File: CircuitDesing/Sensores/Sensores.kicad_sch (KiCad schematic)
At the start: 6 parts

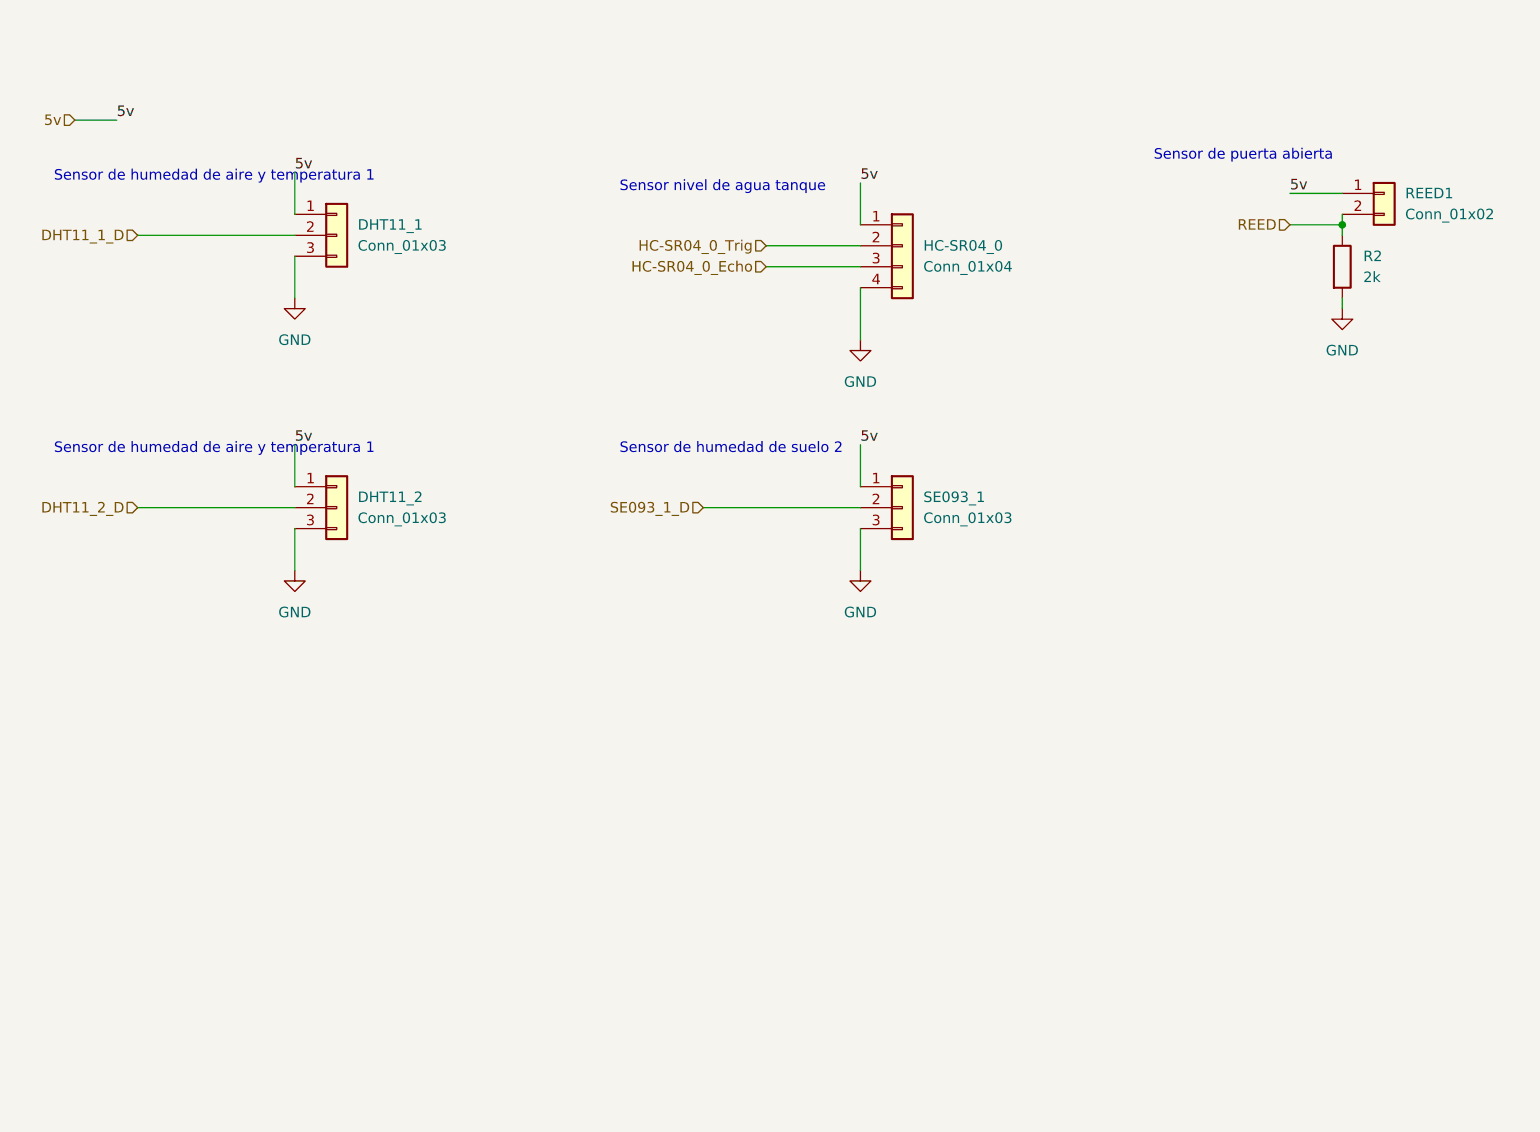
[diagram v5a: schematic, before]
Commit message: Listo para Ruteo
Cambios en programador, led usuario, pines 34 35 (solo entrada)
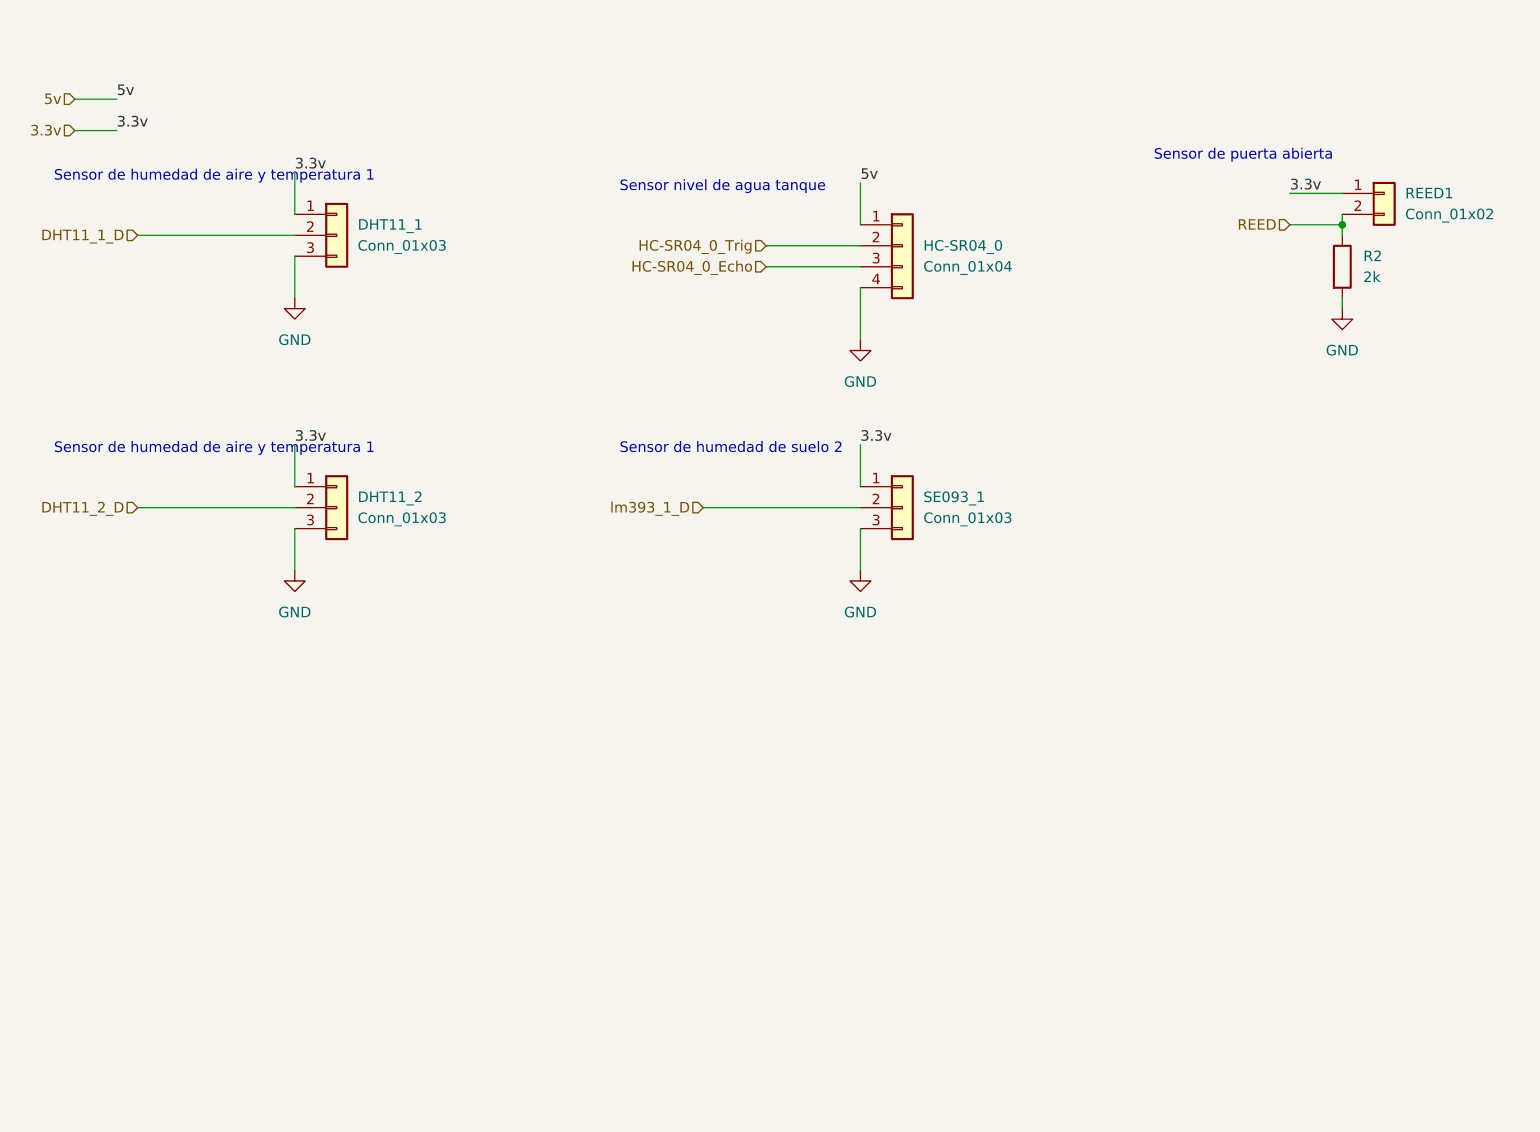
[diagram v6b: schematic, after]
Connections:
- net 5v: no longer DHT11_1.1 (Pin_1), DHT11_2.1 (Pin_1), REED1.1 (Pin_1), SE093_1.1 (Pin_1)
- net SE093_1_D renamed lm393_1_D
- new net 3.3v: DHT11_1.1 (Pin_1), DHT11_2.1 (Pin_1), REED1.1 (Pin_1), SE093_1.1 (Pin_1)
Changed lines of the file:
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@@
+    (stroke (width 0) (type default) (color 0 0 0 0))
+  )
+  (wire (pts (xy 43.18 52.07) (xy 48.26 52.07))
     (stroke (width 0) (type default) (color 0 0 0 0))
   )
@@
     (stroke (width 0) (type default) (color 0 0 0 0))
   )
-  (wire (pts (xy 43.18 50.8) (xy 48.26 50.8))
+  (wire (pts (xy 43.18 48.26) (xy 48.26 48.26))
     (stroke (width 0) (type default) (color 0 0 0 0))
   )
@@
     (effects (font (size 1.27 1.27)) (justify left bottom))
   )
-  (label "5v" (at 48.26 50.8 0)
+  (label "3.3v" (at 48.26 52.07 0)
     (effects (font (size 1.27 1.27)) (justify left bottom))
   )
-  (label "5v" (at 69.85 57.15 0)
+  (label "5v" (at 48.26 48.26 0)
     (effects (font (size 1.27 1.27)) (justify left bottom))
   )
-  (label "5v" (at 69.85 90.17 0)
+  (label "3.3v" (at 69.85 57.15 0)
     (effects (font (size 1.27 1.27)) (justify left bottom))
   )
-  (label "5v" (at 138.43 90.17 0)
+  (label "3.3v" (at 69.85 90.17 0)
     (effects (font (size 1.27 1.27)) (justify left bottom))
   )
-  (label "5v" (at 190.5 59.69 0)
+  (label "3.3v" (at 138.43 90.17 0)
+    (effects (font (size 1.27 1.27)) (justify left bottom))
+  )
+  (label "3.3v" (at 190.5 59.69 0)
     (effects (font (size 1.27 1.27)) (justify left bottom))
   )
@@
     (effects (font (size 1.27 1.27)) (justify right))
   )
-  (hierarchical_label "SE093_1_D" (shape input) (at 119.38 97.79 180)
+  (hierarchical_label "lm393_1_D" (shape input) (at 119.38 97.79 180)
     (effects (font (size 1.27 1.27)) (justify right))
   )
@@
     (effects (font (size 1.27 1.27)) (justify right))
   )
-  (hierarchical_label "5v" (shape input) (at 43.18 50.8 180)
+  (hierarchical_label "5v" (shape input) (at 43.18 48.26 180)
     (effects (font (size 1.27 1.27)) (justify right))
   )
@@
     (effects (font (size 1.27 1.27)) (justify right))
   )
+  (hierarchical_label "3.3v" (shape input) (at 43.18 52.07 180)
+    (effects (font (size 1.27 1.27)) (justify right))
+  )

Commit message: Coversores lógicos + alertas + cambios genrales
Coversores lógicos + alertas + cambios generales
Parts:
- removed HC-SR04_0: Conn_01x04, Connector_JST:JST_EH_B4B-EH-A_1x04_P2.50mm_Vertical, symbol Connector_Generic:Conn_01x04
- added HC-SR?: Conn_01x04, Connector_JST:JST_EH_B4B-EH-A_1x04_P2.50mm_Vertical, symbol Connector_Generic:Conn_01x04
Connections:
- net 5v: now also HC-SR?.1 (Pin_1)
- net GND: now also HC-SR?.4 (Pin_4)
- new net Conversor_NLog5/HV1: HC-SR?.2 (Pin_2)
- new net Conversor_NLog5/HV2: HC-SR?.3 (Pin_3)
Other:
- added sheet Conversor_NLog5 (Con_digital.kicad_sch)
- note added: "Sensor nivel de agua 50%"
- note removed: "Sensor nivel de agua tanque"
- moved on the sheet: DHT11_2, SE093_1

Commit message: Ruteo2.0
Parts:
- gave numbers to parts that had none: 1
- renumbered R2 to R3
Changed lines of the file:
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@@
   (symbol (lib_id "Connector_Generic:Conn_01x04") (at 158.75 101.6 0) (unit 1)
     (in_bom yes) (on_board yes) (fields_autoplaced)
-    (property "Reference" "HC-SR?" (id 0) (at 161.29 101.5999 0)
+    (property "Reference" "HC-SR1" (id 0) (at 161.29 101.5999 0)
       (effects (font (size 1.27 1.27)) (justify left))
     )
@@
   (symbol (lib_id "power:GND") (at 134.62 73.66 0) (unit 1)
     (in_bom yes) (on_board yes) (fields_autoplaced)
-    (property "Reference" "#PWR0107" (id 0) (at 134.62 80.01 0)
+    (property "Reference" "#PWR017" (id 0) (at 134.62 80.01 0)
       (effects (font (size 1.27 1.27)) hide)
     )
@@
   (symbol (lib_id "power:GND") (at 71.12 111.76 0) (unit 1)
     (in_bom yes) (on_board yes) (fields_autoplaced)
-    (property "Reference" "#PWR0106" (id 0) (at 71.12 118.11 0)
+    (property "Reference" "#PWR016" (id 0) (at 71.12 118.11 0)
       (effects (font (size 1.27 1.27)) hide)
     )
@@
   (symbol (lib_id "power:GND") (at 196.85 73.66 0) (unit 1)
     (in_bom yes) (on_board yes) (fields_autoplaced)
-    (property "Reference" "#PWR0109" (id 0) (at 196.85 80.01 0)
+    (property "Reference" "#PWR019" (id 0) (at 196.85 80.01 0)
       (effects (font (size 1.27 1.27)) hide)
     )
@@
   (symbol (lib_id "power:GND") (at 153.67 111.76 0) (unit 1)
     (in_bom yes) (on_board yes) (fields_autoplaced)
-    (property "Reference" "#PWR?" (id 0) (at 153.67 118.11 0)
+    (property "Reference" "#PWR018" (id 0) (at 153.67 118.11 0)
       (effects (font (size 1.27 1.27)) hide)
     )
@@
   (symbol (lib_id "power:GND") (at 69.85 72.39 0) (unit 1)
     (in_bom yes) (on_board yes) (fields_autoplaced)
-    (property "Reference" "#PWR0108" (id 0) (at 69.85 78.74 0)
+    (property "Reference" "#PWR015" (id 0) (at 69.85 78.74 0)
       (effects (font (size 1.27 1.27)) hide)
     )
@@
   (symbol (lib_id "Device:R") (at 196.85 68.58 0) (unit 1)
     (in_bom yes) (on_board yes) (fields_autoplaced)
-    (property "Reference" "R2" (id 0) (at 199.39 67.3099 0)
+    (property "Reference" "R3" (id 0) (at 199.39 67.3099 0)
       (effects (font (size 1.27 1.27)) (justify left))
     )
